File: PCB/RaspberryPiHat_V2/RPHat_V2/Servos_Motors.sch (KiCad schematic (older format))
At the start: 10 parts

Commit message: Schematic clean-up
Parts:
- added D?: LED, symbol Device:LED
- added R?: 4.7k, symbol Device:R
- added SW?: SW_DPDT_x2, symbol Switch:SW_DPDT_x2
- added U?: Teensy4.0, symbol RPHat_V2-rescue:Teensy4.0-teensy
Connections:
- net +5V: now also SW?.1 (A)
- net GNDREF: now also R?.2, U?.1 (GND)
- net Neopixels_1: now also U?.39 (28_RX7)
- net Neopixels_2: now also U?.40 (29_TX7)
- net PWM_Left: now also U?.5 (3_LRCLK2)
- net PWM_Right: now also U?.4 (2_OUT2)
- net PWMservo_1: now also U?.6 (4_BCLK2)
- net PWMservo_2: now also U?.7 (5_IN2)
- net PWMservo_3: now also U?.8 (6_OUT1D)
- net PWMservo_4: now also U?.9 (7_RX2_OUT1A)
- net PWMservo_5: now also U?.10 (8_TX2_IN1)
- net PWMservo_6: now also U?.11 (9_OUT1C)
- new net: D?.2 (A), SW?.2 (B), U?.33 (VIN)
- new net: D?.1 (K), R?.1
- new net Teensy_Uart_RX: U?.2 (0_RX1_CRX2_CS1)
- new net Teensy_Uart_TX: U?.3 (1_TX1_CTX2_MISO1)
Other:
- moved on the sheet: J?

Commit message: Started routing PCB
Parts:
- gave numbers to parts that had none: 14
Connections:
- net SDA: now reaches U6.25 (18_A4_SDA0)
- net SCL: now reaches U6.26 (19_A5_SCL0)
- net Teensy_Uart_RX: no longer names the net of U6.2 (0_RX1_CRX2_CS1)
- net Teensy_Uart_TX: no longer names the net of U6.3 (1_TX1_CTX2_MISO1)

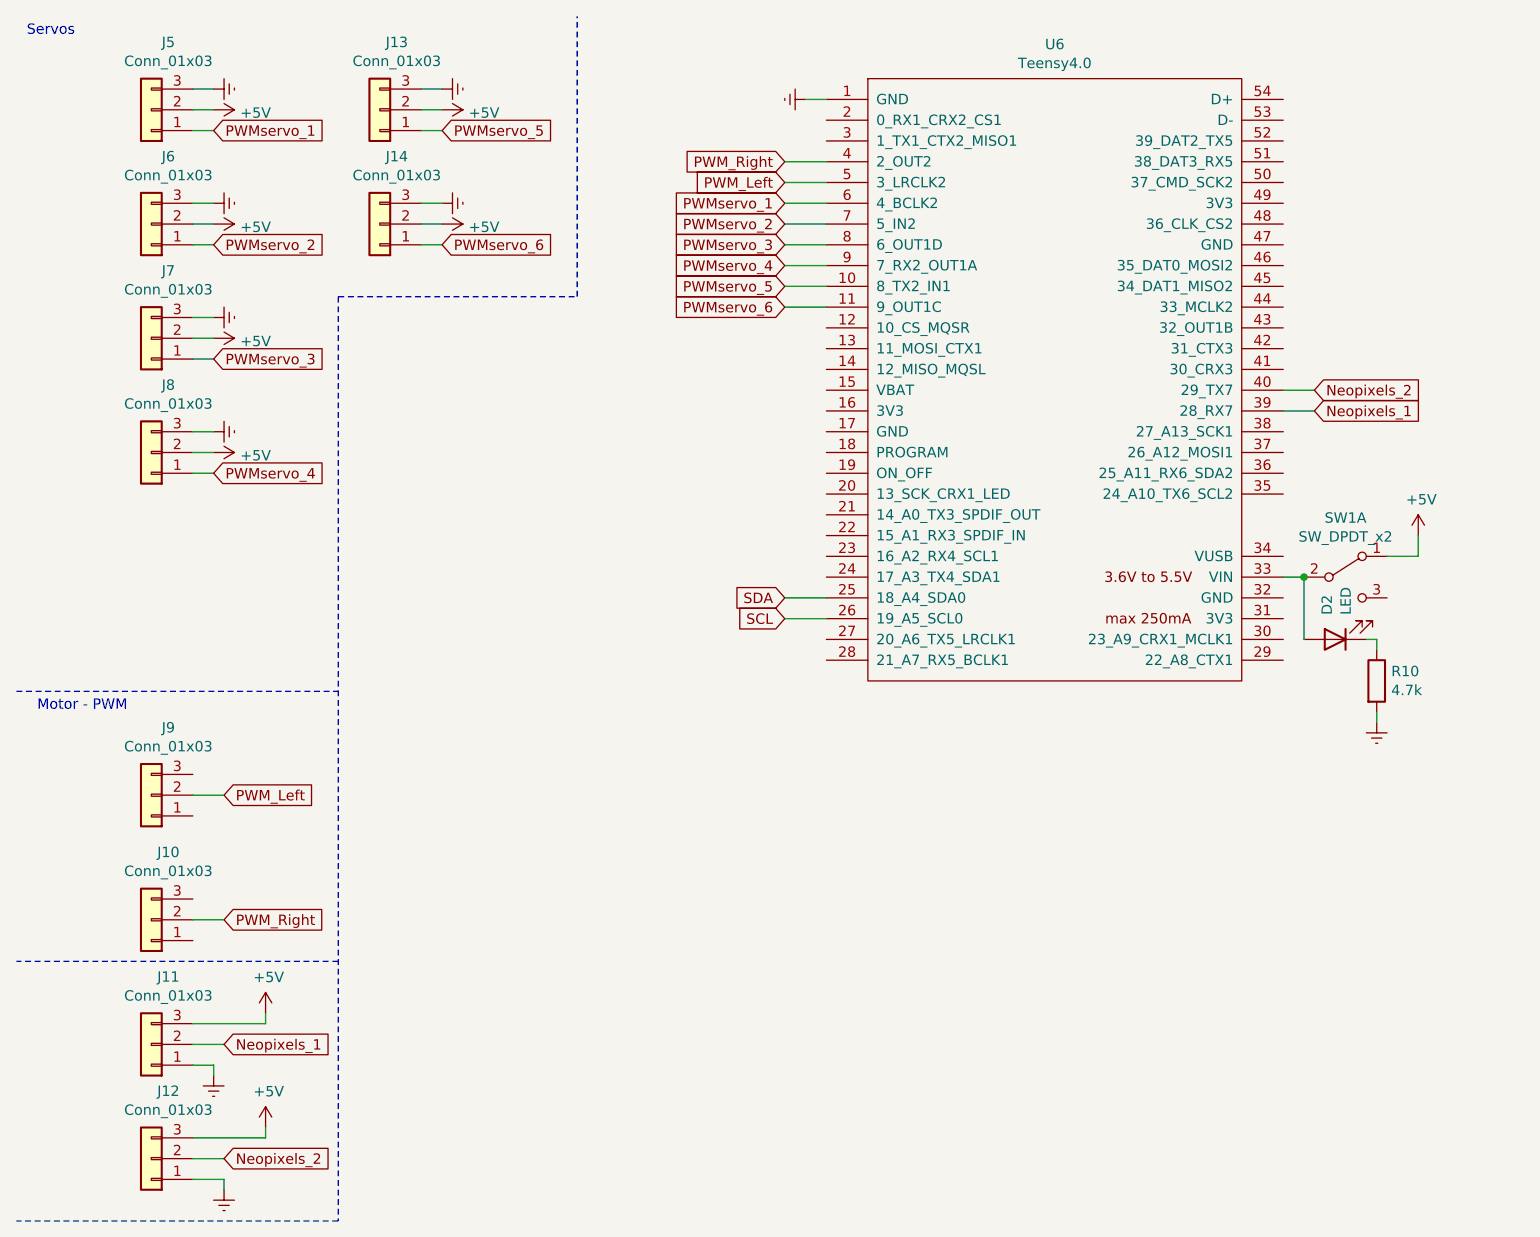
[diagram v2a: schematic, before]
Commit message: Added footprints to all componetns
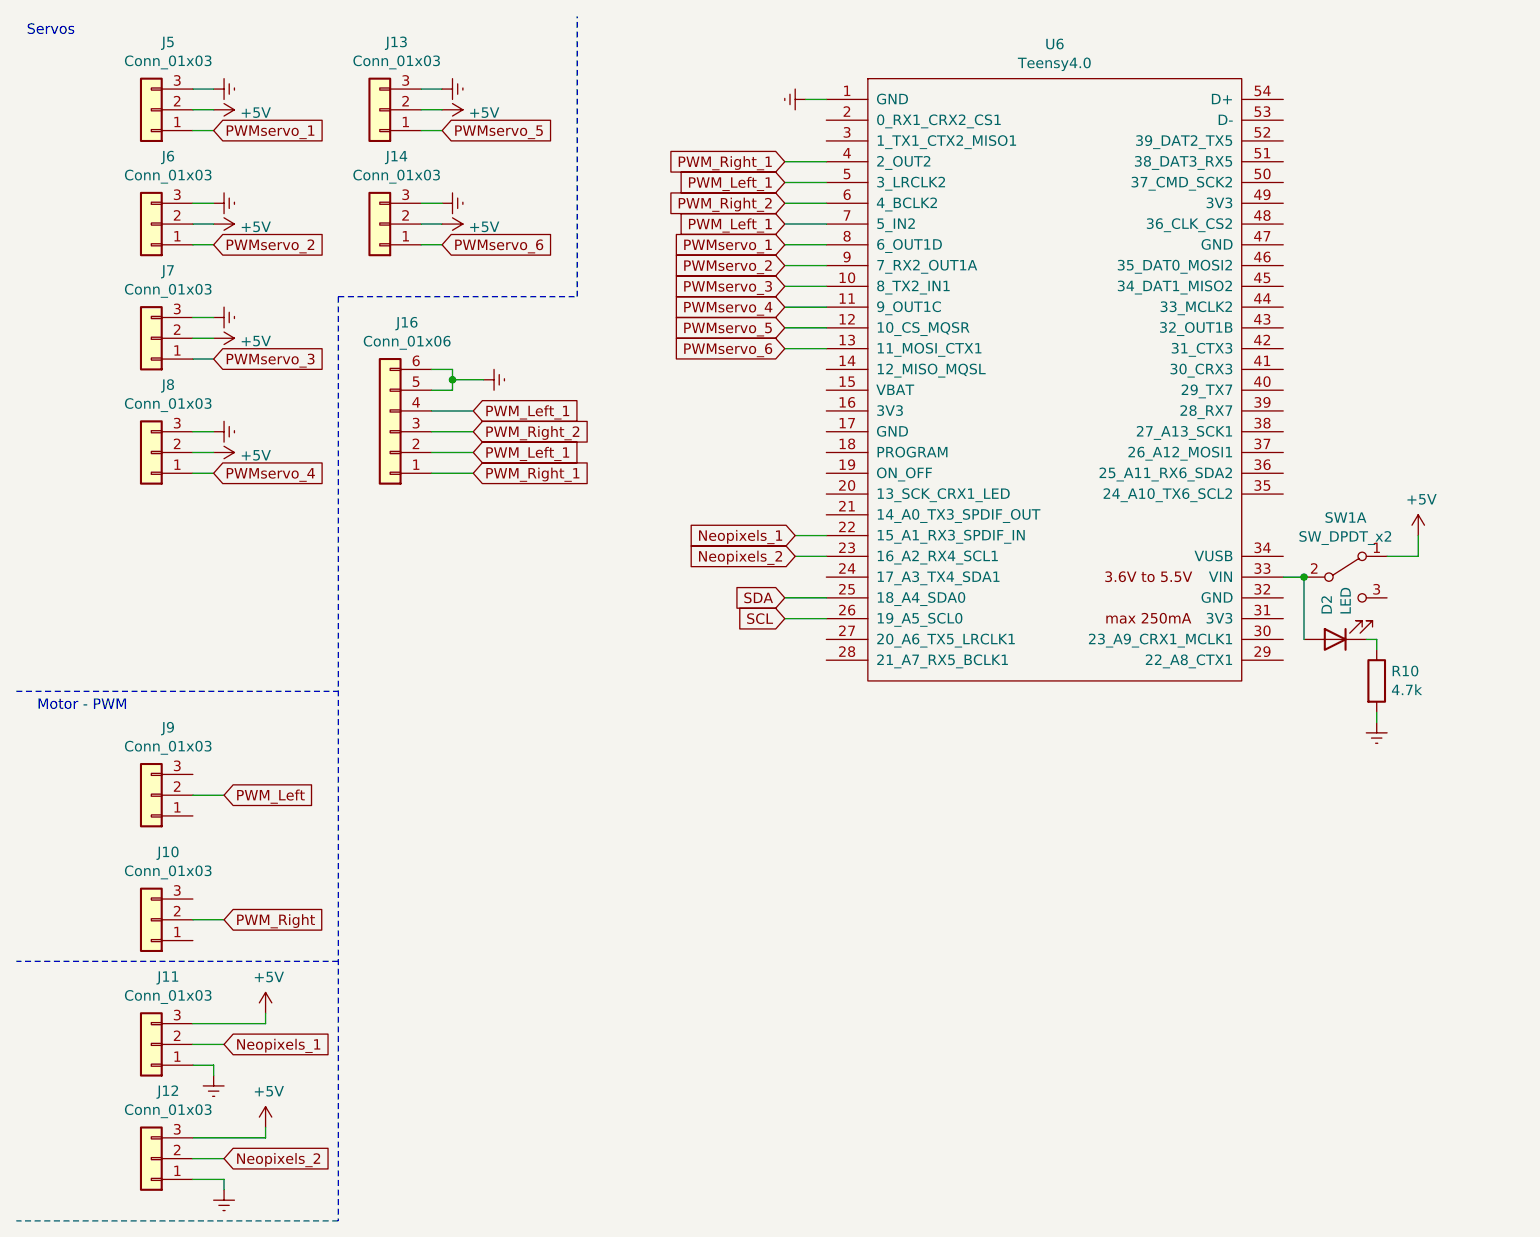
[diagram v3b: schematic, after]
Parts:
- added J16: Conn_01x06, Connector_PinHeader_2.54mm:PinHeader_1x06_P2.54mm_Horizontal, symbol Connector_Generic:Conn_01x06
- D2, R10: footprint (none) -> Resistor_SMD:R_0603_1608Metric_Pad0.98x0.95mm_HandSolder
- SW1: footprint (none) -> Connector_PinHeader_2.54mm:PinHeader_1x03_P2.54mm_Vertical
- U6: footprint (none) -> teensy:Teensy40
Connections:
- net GNDREF: now also J16.5 (Pin_5), J16.6 (Pin_6)
- net Neopixels_1: now also U6.22 (15_A1_RX3_SPDIF_IN); no longer U6.39 (28_RX7)
- net Neopixels_2: now also U6.23 (16_A2_RX4_SCL1); no longer U6.40 (29_TX7)
- net PWM_Left: no longer U6.5 (3_LRCLK2)
- net PWM_Right: no longer U6.4 (2_OUT2)
- net PWMservo_1: now also U6.8 (6_OUT1D); no longer U6.6 (4_BCLK2)
- net PWMservo_2: now also U6.9 (7_RX2_OUT1A); no longer U6.7 (5_IN2)
- net PWMservo_3: now also U6.10 (8_TX2_IN1); no longer U6.8 (6_OUT1D)
- net PWMservo_4: now also U6.11 (9_OUT1C); no longer U6.9 (7_RX2_OUT1A)
- net PWMservo_5: now also U6.12 (10_CS_MQSR); no longer U6.10 (8_TX2_IN1)
- net PWMservo_6: now also U6.13 (11_MOSI_CTX1); no longer U6.11 (9_OUT1C)
- new net PWM_Left_1: J16.2 (Pin_2), J16.4 (Pin_4), U6.5 (3_LRCLK2), U6.7 (5_IN2)
- new net PWM_Right_1: J16.1 (Pin_1), U6.4 (2_OUT2)
- new net PWM_Right_2: J16.3 (Pin_3), U6.6 (4_BCLK2)
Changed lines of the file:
@@
 F 0 "U6" H 5500 3865 50  0000 C CNN
 F 1 "Teensy4.0" H 5500 3774 50  0000 C CNN
-F 2 "" H 5100 2450 50  0001 C CNN
+F 2 "teensy:Teensy40" H 5100 2450 50  0001 C CNN
 F 3 "" H 5100 2450 50  0001 C CNN
 	1    5500 2250
@@
 F 0 "SW1" H 6900 3485 50  0000 C CNN
 F 1 "SW_DPDT_x2" H 6900 3394 50  0000 C CNN
-F 2 "" H 6900 3200 50  0001 C CNN
+F 2 "Connector_PinHeader_2.54mm:PinHeader_1x03_P2.54mm_Vertical" H 6900 3200 50  0001 C CNN
 F 3 "~" H 6900 3200 50  0001 C CNN
 	1    6900 3200
@@
 F 0 "D2" V 6889 3382 50  0000 R CNN
 F 1 "LED" V 6798 3382 50  0000 R CNN
-F 2 "" H 6850 3500 50  0001 C CNN
+F 2 "Resistor_SMD:R_0603_1608Metric_Pad0.98x0.95mm_HandSolder" H 6850 3500 50  0001 C CNN
 F 3 "~" H 6850 3500 50  0001 C CNN
 	1    6850 3500
@@
 F 0 "R10" H 7120 3746 50  0000 L CNN
 F 1 "4.7k" H 7120 3655 50  0000 L CNN
-F 2 "" V 6980 3700 50  0001 C CNN
+F 2 "Resistor_SMD:R_0603_1608Metric_Pad0.98x0.95mm_HandSolder" V 6980 3700 50  0001 C CNN
 F 3 "~" H 7050 3700 50  0001 C CNN
 	1    7050 3700
@@
 	7000 3500 7050 3500
 Text GLabel 4200 1200 0    50   Input ~ 0
-PWM_Right
+PWM_Right_1
 Text GLabel 4200 1300 0    50   Input ~ 0
-PWM_Left
+PWM_Left_1
 Wire Wire Line
 	4200 1300 4400 1300
 Wire Wire Line
 	4200 1200 4400 1200
-Text GLabel 4200 1400 0    50   Input ~ 0
+Text GLabel 4200 1600 0    50   Input ~ 0
 PWMservo_1
-Text GLabel 6750 2400 2    50   Input ~ 0
-Neopixels_1
-Text GLabel 4200 1500 0    50   Input ~ 0
+Text GLabel 4200 1700 0    50   Input ~ 0
 PWMservo_2
-Text GLabel 4200 1600 0    50   Input ~ 0
+Text GLabel 4200 1800 0    50   Input ~ 0
 PWMservo_3
-Text GLabel 4200 1700 0    50   Input ~ 0
+Text GLabel 4200 1900 0    50   Input ~ 0
 PWMservo_4
-Text GLabel 4200 1800 0    50   Input ~ 0
+Text GLabel 4200 2000 0    50   Input ~ 0
 PWMservo_5
-Text GLabel 4200 1900 0    50   Input ~ 0
+Text GLabel 4200 2100 0    50   Input ~ 0
 PWMservo_6
-Text GLabel 6750 2300 2    50   Input ~ 0
-Neopixels_2
 $Comp
 L power:GNDREF #PWR?
@@
 	4400 900  4300 900
 Wire Wire Line
-	4200 1400 4400 1400
-Wire Wire Line
-	4200 1500 4400 1500
-Wire Wire Line
 	4200 1600 4400 1600
 Wire Wire Line
@@
 	4200 1900 4400 1900
 Wire Wire Line
-	6750 2300 6600 2300
-Wire Wire Line
-	6750 2400 6600 2400
+	4200 2000 4400 2000
+Wire Wire Line
+	4200 2100 4400 2100
 Text GLabel 4200 3300 0    50   Input ~ 0
 SDA
@@
 Wire Wire Line
 	4200 3400 4400 3400
+Text GLabel 4200 1400 0    50   Input ~ 0
+PWM_Right_2
+Text GLabel 4200 1500 0    50   Input ~ 0
+PWM_Left_1
+Wire Wire Line
+	4200 1500 4400 1500
+Wire Wire Line
+	4200 1400 4400 1400
+$Comp
+L Connector_Generic:Conn_01x06 J16
+U 1 1 60B35E0D
+P 2300 2500
+F 0 "J16" H 2218 1975 50  0000 C CNN
+F 1 "Conn_01x06" H 2218 2066 50  0000 C CNN
+F 2 "Connector_PinHeader_2.54mm:PinHeader_1x06_P2.54mm_Horizontal" H 2300 2500 50  0001 C CNN
+F 3 "~" H 2300 2500 50  0001 C CNN
+	1    2300 2500
+	-1   0    0    1
+$EndComp
+Text GLabel 2700 2700 2    50   Input ~ 0
+PWM_Right_1
+Text GLabel 2700 2600 2    50   Input ~ 0
+PWM_Left_1
+Wire Wire Line
+	2700 2600 2500 2600
+Wire Wire Line
+	2700 2700 2500 2700
+Text GLabel 2700 2500 2    50   Input ~ 0
+PWM_Right_2
+Text GLabel 2700 2400 2    50   Input ~ 0
+PWM_Left_1
+Wire Wire Line
+	2700 2400 2500 2400
+Wire Wire Line
+	2700 2500 2500 2500
+$Comp
+L power:GNDREF #PWR03
+U 1 1 60B40966
+P 2750 2250
+F 0 "#PWR03" H 2750 2000 50  0001 C CNN
+F 1 "GNDREF" V 2755 2122 50  0001 R CNN
+F 2 "" H 2750 2250 50  0001 C CNN
+F 3 "" H 2750 2250 50  0001 C CNN
+	1    2750 2250
+	0    -1   -1   0
+$EndComp
+Wire Wire Line
+	2500 2200 2600 2200
+Wire Wire Line
+	2600 2200 2600 2250
+Wire Wire Line
+	2600 2250 2750 2250
+Wire Wire Line
+	2500 2300 2600 2300
+Wire Wire Line
+	2600 2300 2600 2250
+Connection ~ 2600 2250
+Text GLabel 4250 3000 0    50   Input ~ 0
+Neopixels_1
+Text GLabel 4250 3100 0    50   Input ~ 0
+Neopixels_2
+Wire Wire Line
+	4250 3100 4400 3100
+Wire Wire Line
+	4250 3000 4400 3000
 $EndSCHEMATC

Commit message: Continued working on the pcb
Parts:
- J10, J11, J12, J5, J9: footprint Connector_PinHeader_2.54mm:PinHeader_1x03_P2.54mm_Horizontal -> Connector_PinHeader_2.54mm:PinHeader_1x03_P2.54mm_Vertical
- J16: footprint Connector_PinHeader_2.54mm:PinHeader_1x06_P2.54mm_Horizontal -> Connector_PinHeader_2.54mm:PinHeader_1x06_P2.54mm_Vertical
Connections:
- net GNDREF: now also U6.32 (GND)
- net +3V3: now reaches U6.31 (3V3)
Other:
- moved on the sheet: D2, R10, SW1A
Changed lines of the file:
@@
 F 0 "J5" H 1068 625 50  0000 C CNN
 F 1 "Conn_01x03" H 1068 716 50  0000 C CNN
-F 2 "Connector_PinHeader_2.54mm:PinHeader_1x03_P2.54mm_Horizontal" H 1150 950 50  0001 C CNN
+F 2 "Connector_PinHeader_2.54mm:PinHeader_1x03_P2.54mm_Vertical" H 1150 950 50  0001 C CNN
 F 3 "~" H 1150 950 50  0001 C CNN
 	1    1150 950
@@
 F 0 "J9" H 1068 3925 50  0000 C CNN
 F 1 "Conn_01x03" H 1068 4016 50  0000 C CNN
-F 2 "Connector_PinHeader_2.54mm:PinHeader_1x03_P2.54mm_Horizontal" H 1150 4250 50  0001 C CNN
+F 2 "Connector_PinHeader_2.54mm:PinHeader_1x03_P2.54mm_Vertical" H 1150 4250 50  0001 C CNN
 F 3 "~" H 1150 4250 50  0001 C CNN
 	1    1150 4250
@@
 F 0 "J10" H 1068 4525 50  0000 C CNN
 F 1 "Conn_01x03" H 1068 4616 50  0000 C CNN
-F 2 "Connector_PinHeader_2.54mm:PinHeader_1x03_P2.54mm_Horizontal" H 1150 4850 50  0001 C CNN
+F 2 "Connector_PinHeader_2.54mm:PinHeader_1x03_P2.54mm_Vertical" H 1150 4850 50  0001 C CNN
 F 3 "~" H 1150 4850 50  0001 C CNN
 	1    1150 4850
@@
 F 0 "J11" H 1068 5125 50  0000 C CNN
 F 1 "Conn_01x03" H 1068 5216 50  0000 C CNN
-F 2 "Connector_PinHeader_2.54mm:PinHeader_1x03_P2.54mm_Horizontal" H 1150 5450 50  0001 C CNN
+F 2 "Connector_PinHeader_2.54mm:PinHeader_1x03_P2.54mm_Vertical" H 1150 5450 50  0001 C CNN
 F 3 "~" H 1150 5450 50  0001 C CNN
 	1    1150 5450
@@
 F 0 "J12" H 1068 5675 50  0000 C CNN
 F 1 "Conn_01x03" H 1068 5766 50  0000 C CNN
-F 2 "Connector_PinHeader_2.54mm:PinHeader_1x03_P2.54mm_Horizontal" H 1150 6000 50  0001 C CNN
+F 2 "Connector_PinHeader_2.54mm:PinHeader_1x03_P2.54mm_Vertical" H 1150 6000 50  0001 C CNN
 F 3 "~" H 1150 6000 50  0001 C CNN
 	1    1150 6000
@@
 L Switch:SW_DPDT_x2 SW?
 U 1 1 60B9F9A5
-P 6900 3200
+P 7300 3200
 AR Path="/60B9F9A5" Ref="SW?"  Part="1"
 AR Path="/609A082B/60B9F9A5" Ref="SW1"  Part="1"
-F 0 "SW1" H 6900 3485 50  0000 C CNN
-F 1 "SW_DPDT_x2" H 6900 3394 50  0000 C CNN
-F 2 "Connector_PinHeader_2.54mm:PinHeader_1x03_P2.54mm_Vertical" H 6900 3200 50  0001 C CNN
-F 3 "~" H 6900 3200 50  0001 C CNN
-	1    6900 3200
+F 0 "SW1" H 7300 3485 50  0000 C CNN
+F 1 "SW_DPDT_x2" H 7300 3394 50  0000 C CNN
+F 2 "Connector_PinHeader_2.54mm:PinHeader_1x03_P2.54mm_Vertical" H 7300 3200 50  0001 C CNN
+F 3 "~" H 7300 3200 50  0001 C CNN
+	1    7300 3200
 	1    0    0    -1
 $EndComp
@@
 L power:+5V #PWR?
 U 1 1 60B9F9AB
-P 7250 3000
+P 7650 3000
 AR Path="/60B9F9AB" Ref="#PWR?"  Part="1"
 AR Path="/609A082B/60B9F9AB" Ref="#PWR0159"  Part="1"
-F 0 "#PWR0159" H 7250 2850 50  0001 C CNN
-F 1 "+5V" H 7265 3173 50  0000 C CNN
-F 2 "" H 7250 3000 50  0001 C CNN
-F 3 "" H 7250 3000 50  0001 C CNN
-	1    7250 3000
-	1    0    0    -1
-$EndComp
-Wire Wire Line
-	7100 3100 7250 3100
-Wire Wire Line
-	7250 3100 7250 3000
-Wire Wire Line
-	6700 3200 6600 3200
+F 0 "#PWR0159" H 7650 2850 50  0001 C CNN
+F 1 "+5V" H 7665 3173 50  0000 C CNN
+F 2 "" H 7650 3000 50  0001 C CNN
+F 3 "" H 7650 3000 50  0001 C CNN
+	1    7650 3000
+	1    0    0    -1
+$EndComp
+Wire Wire Line
+	7500 3100 7650 3100
+Wire Wire Line
+	7650 3100 7650 3000
 $Comp
 L Device:LED D?
 U 1 1 60B9F9B4
-P 6850 3500
+P 7250 3500
 AR Path="/60B9F9B4" Ref="D?"  Part="1"
 AR Path="/609A082B/60B9F9B4" Ref="D2"  Part="1"
-F 0 "D2" V 6889 3382 50  0000 R CNN
-F 1 "LED" V 6798 3382 50  0000 R CNN
-F 2 "Resistor_SMD:R_0603_1608Metric_Pad0.98x0.95mm_HandSolder" H 6850 3500 50  0001 C CNN
-F 3 "~" H 6850 3500 50  0001 C CNN
-	1    6850 3500
-	-1   0    0    1
-$EndComp
-Connection ~ 6700 3200
+F 0 "D2" V 7289 3382 50  0000 R CNN
+F 1 "LED" V 7198 3382 50  0000 R CNN
+F 2 "Resistor_SMD:R_0603_1608Metric_Pad0.98x0.95mm_HandSolder" H 7250 3500 50  0001 C CNN
+F 3 "~" H 7250 3500 50  0001 C CNN
+	1    7250 3500
+	-1   0    0    1
+$EndComp
+Connection ~ 7100 3200
 $Comp
 L Device:R R?
 U 1 1 60B9F9BB
-P 7050 3700
+P 7450 3700
 AR Path="/60B9F9BB" Ref="R?"  Part="1"
 AR Path="/609A082B/60B9F9BB" Ref="R10"  Part="1"
-F 0 "R10" H 7120 3746 50  0000 L CNN
-F 1 "4.7k" H 7120 3655 50  0000 L CNN
-F 2 "Resistor_SMD:R_0603_1608Metric_Pad0.98x0.95mm_HandSolder" V 6980 3700 50  0001 C CNN
-F 3 "~" H 7050 3700 50  0001 C CNN
-	1    7050 3700
-	1    0    0    -1
-$EndComp
-Wire Wire Line
-	7050 3500 7050 3550
+F 0 "R10" H 7520 3746 50  0000 L CNN
+F 1 "4.7k" H 7520 3655 50  0000 L CNN
+F 2 "Resistor_SMD:R_0603_1608Metric_Pad0.98x0.95mm_HandSolder" V 7380 3700 50  0001 C CNN
+F 3 "~" H 7450 3700 50  0001 C CNN
+	1    7450 3700
+	1    0    0    -1
+$EndComp
+Wire Wire Line
+	7450 3500 7450 3550
 $Comp
 L power:GNDREF #PWR?
 U 1 1 60B9F9C2
-P 7050 3900
+P 7450 3900
 AR Path="/60B9F9C2" Ref="#PWR?"  Part="1"
 AR Path="/609A082B/60B9F9C2" Ref="#PWR0160"  Part="1"
-F 0 "#PWR0160" H 7050 3650 50  0001 C CNN
-F 1 "GNDREF" H 7055 3727 50  0001 C CNN
-F 2 "" H 7050 3900 50  0001 C CNN
-F 3 "" H 7050 3900 50  0001 C CNN
-	1    7050 3900
-	1    0    0    -1
-$EndComp
-Wire Wire Line
-	7050 3850 7050 3900
-Wire Wire Line
-	6700 3500 6700 3200
-Wire Wire Line
-	7000 3500 7050 3500
+F 0 "#PWR0160" H 7450 3650 50  0001 C CNN
+F 1 "GNDREF" H 7455 3727 50  0001 C CNN
+F 2 "" H 7450 3900 50  0001 C CNN
+F 3 "" H 7450 3900 50  0001 C CNN
+	1    7450 3900
+	1    0    0    -1
+$EndComp
+Wire Wire Line
+	7450 3850 7450 3900
+Wire Wire Line
+	7100 3500 7100 3200
+Wire Wire Line
+	7400 3500 7450 3500
 Text GLabel 4200 1200 0    50   Input ~ 0
 PWM_Right_1
@@
 F 0 "J16" H 2218 1975 50  0000 C CNN
 F 1 "Conn_01x06" H 2218 2066 50  0000 C CNN
-F 2 "Connector_PinHeader_2.54mm:PinHeader_1x06_P2.54mm_Horizontal" H 2300 2500 50  0001 C CNN
+F 2 "Connector_PinHeader_2.54mm:PinHeader_1x06_P2.54mm_Vertical" H 2300 2500 50  0001 C CNN
 F 3 "~" H 2300 2500 50  0001 C CNN
 	1    2300 2500
@@
 Wire Wire Line
 	4250 3000 4400 3000
+$Comp
+L power:+3V3 #PWR0132
+U 1 1 60B34CA4
+P 6650 3400
+F 0 "#PWR0132" H 6650 3250 50  0001 C CNN
+F 1 "+3V3" V 6665 3528 50  0000 L CNN
+F 2 "" H 6650 3400 50  0001 C CNN
+F 3 "" H 6650 3400 50  0001 C CNN
+	1    6650 3400
+	0    1    1    0
+$EndComp
+$Comp
+L power:GNDREF #PWR0138
+U 1 1 60B355B2
+P 6650 3300
+F 0 "#PWR0138" H 6650 3050 50  0001 C CNN
+F 1 "GNDREF" V 6655 3172 50  0000 R CNN
+F 2 "" H 6650 3300 50  0001 C CNN
+F 3 "" H 6650 3300 50  0001 C CNN
+	1    6650 3300
+	0    -1   -1   0
+$EndComp
+Wire Wire Line
+	6650 3300 6600 3300
+Wire Wire Line
+	6650 3400 6600 3400
+Wire Wire Line
+	6600 3200 7100 3200
 $EndSCHEMATC
